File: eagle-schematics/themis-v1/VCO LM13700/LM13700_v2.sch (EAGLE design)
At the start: 39 parts

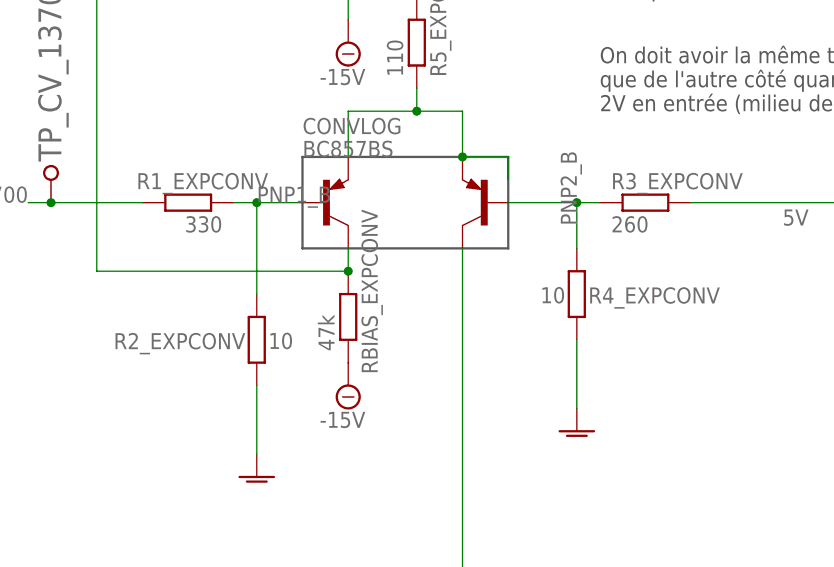
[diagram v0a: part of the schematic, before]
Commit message: bug fix on LM13700 schematics
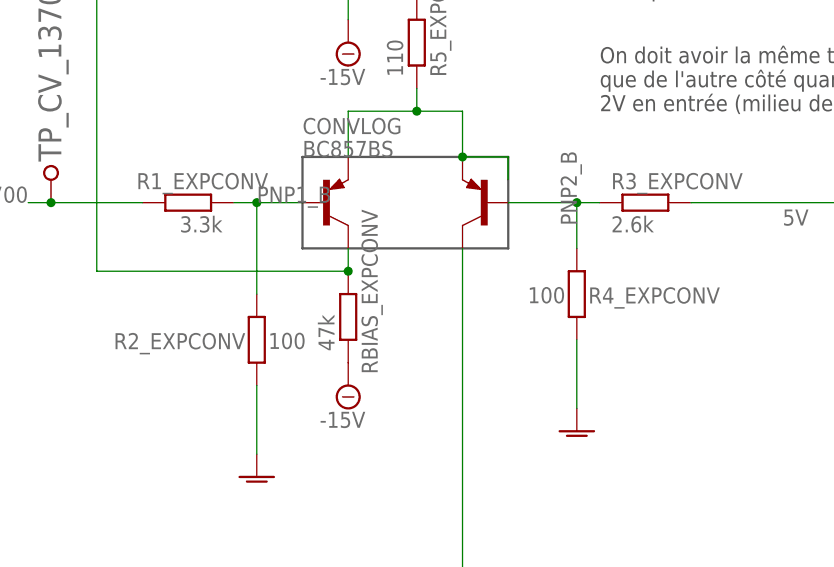
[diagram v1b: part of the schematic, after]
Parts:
- R1_EXPCONV: value 330 -> 3.3k
- R2_EXPCONV, R4_EXPCONV: value 10 -> 100
- R3_EXPCONV: value 260 -> 2.6k

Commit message: bug fix
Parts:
- R3_EXPCONV: value 2.6k -> 8.2k
- R5_EXPCONV: value 110 -> 220
- REE_13700: value 27k -> 47k
- RTRI_13700: value 12k -> 10k
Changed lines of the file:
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@@
 <part name="R1_EXPCONV" library="rcl" library_urn="urn:adsk.eagle:library:334" deviceset="R-EU_" device="0204/7" package3d_urn="urn:adsk.eagle:package:23498/2" value="3.3k"/>
 <part name="R2_EXPCONV" library="rcl" library_urn="urn:adsk.eagle:library:334" deviceset="R-EU_" device="0204/7" package3d_urn="urn:adsk.eagle:package:23498/2" value="100"/>
-<part name="R5_EXPCONV" library="rcl" library_urn="urn:adsk.eagle:library:334" deviceset="R-EU_" device="0204/7" package3d_urn="urn:adsk.eagle:package:23498/2" value="110"/>
+<part name="R5_EXPCONV" library="rcl" library_urn="urn:adsk.eagle:library:334" deviceset="R-EU_" device="0204/7" package3d_urn="urn:adsk.eagle:package:23498/2" value="220"/>
 <part name="RBIAS_EXPCONV" library="rcl" library_urn="urn:adsk.eagle:library:334" deviceset="R-EU_" device="0204/7" package3d_urn="urn:adsk.eagle:package:23498/2" value="47k"/>
 <part name="R4_EXPCONV" library="rcl" library_urn="urn:adsk.eagle:library:334" deviceset="R-EU_" device="0204/7" package3d_urn="urn:adsk.eagle:package:23498/2" value="100"/>
-<part name="R3_EXPCONV" library="rcl" library_urn="urn:adsk.eagle:library:334" deviceset="R-EU_" device="0204/7" package3d_urn="urn:adsk.eagle:package:23498/2" value="2.6k"/>
+<part name="R3_EXPCONV" library="rcl" library_urn="urn:adsk.eagle:library:334" deviceset="R-EU_" device="0204/7" package3d_urn="urn:adsk.eagle:package:23498/2" value="8.2k"/>
 <part name="AGND15" library="supply1" library_urn="urn:adsk.eagle:library:371" deviceset="AGND" device=""/>
 <part name="AGND16" library="supply1" library_urn="urn:adsk.eagle:library:371" deviceset="AGND" device=""/>
@@
 <part name="TP_CV_13700" library="6P1_EVB" deviceset="TESTPOINT" device=""/>
 <part name="VCO13700" library="ota" deviceset="LM13700" device="N" value="LM13700N"/>
-<part name="REE_13700" library="rcl" library_urn="urn:adsk.eagle:library:334" deviceset="R-EU_" device="0204/7" package3d_urn="urn:adsk.eagle:package:23498/2" value="27k"/>
-<part name="RTRI_13700" library="rcl" library_urn="urn:adsk.eagle:library:334" deviceset="R-EU_" device="0204/7" package3d_urn="urn:adsk.eagle:package:23498/2" value="12k"/>
+<part name="REE_13700" library="rcl" library_urn="urn:adsk.eagle:library:334" deviceset="R-EU_" device="0204/7" package3d_urn="urn:adsk.eagle:package:23498/2" value="47k"/>
+<part name="RTRI_13700" library="rcl" library_urn="urn:adsk.eagle:library:334" deviceset="R-EU_" device="0204/7" package3d_urn="urn:adsk.eagle:package:23498/2" value="10k"/>
 <part name="RA_13700" library="rcl" library_urn="urn:adsk.eagle:library:334" deviceset="R-EU_" device="0204/7" package3d_urn="urn:adsk.eagle:package:23498/2" value="4.7k"/>
 <part name="RSQU_13700" library="rcl" library_urn="urn:adsk.eagle:library:334" deviceset="R-EU_" device="0204/7" package3d_urn="urn:adsk.eagle:package:23498/2" value="10k"/>
